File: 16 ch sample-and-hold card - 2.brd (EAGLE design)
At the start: 64 x 25.4 mm, 80 parts, among them IC1 TL074D, IC3 TL074D, IC4 TL074D, IC7 TL074D, IC9 MAX306CWI

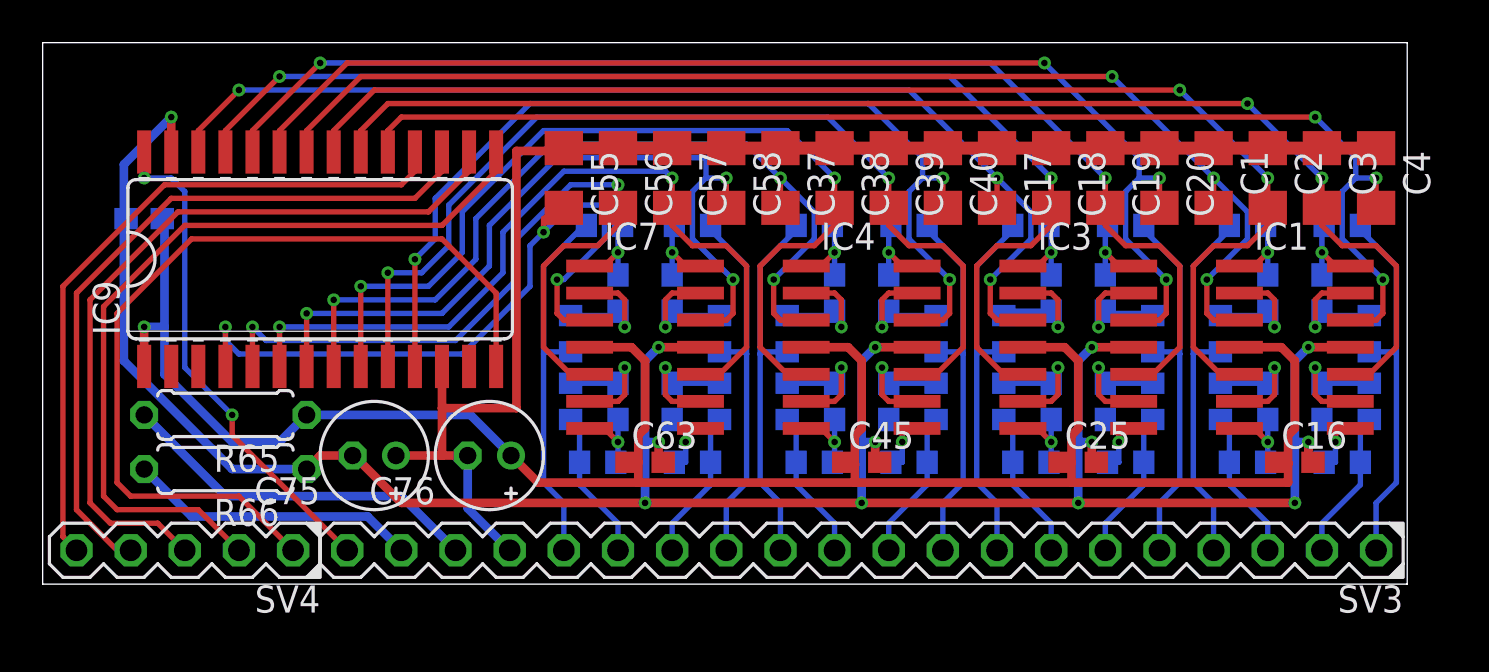
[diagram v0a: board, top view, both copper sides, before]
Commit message: Reworked resistor and electrolytic caps placement to tap power AFTER caps for better noise filtering
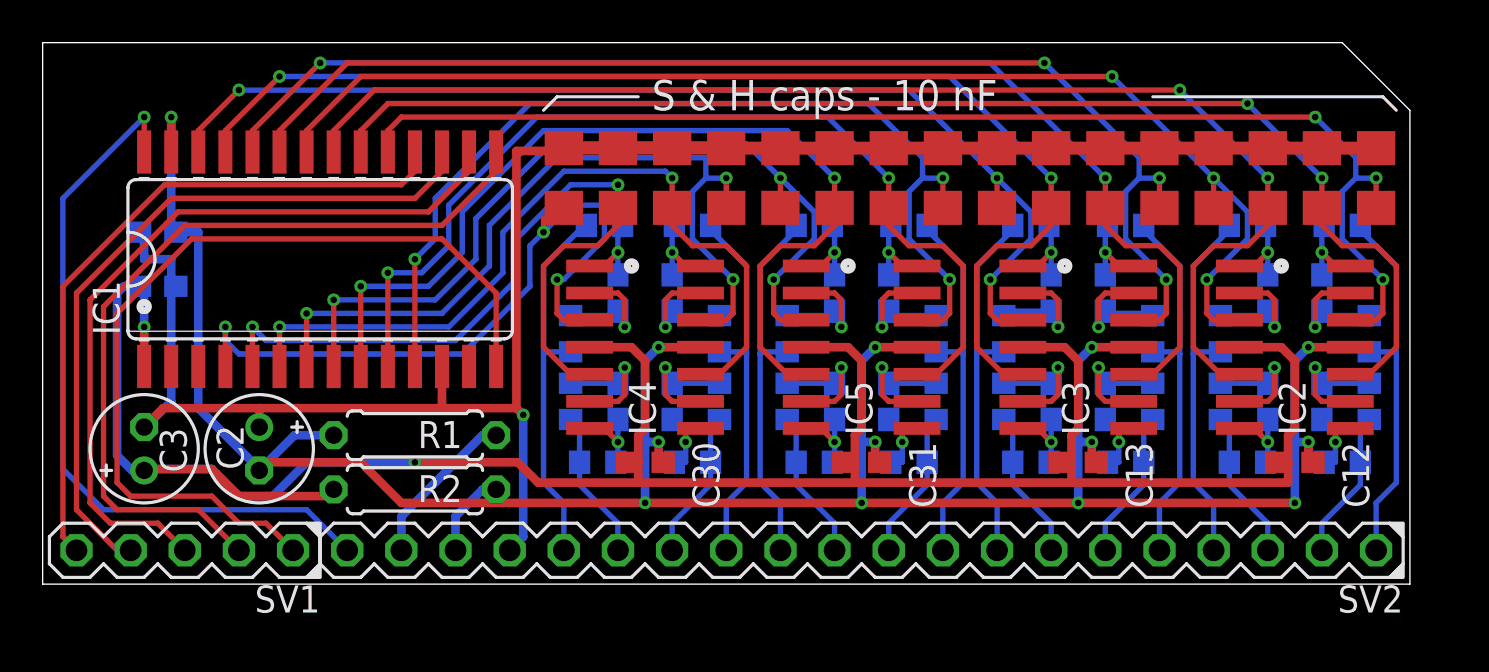
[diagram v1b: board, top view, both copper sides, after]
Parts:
- removed C41, C42, C43, C60, C61, C73: 0.1uF, resistor:C0603
- removed C55, C56, C57, C58: (no value), resistor:C1206
- removed C75, C76: 22uF 25V, resistor:E2-5
- removed IC7: TL074D, linear:SO14
- removed IC9: MAX306CWI, maxim:SO28L
- removed R51, R53, R56: 100R, resistor:R0603
- removed R52, R54, R55: 1k, resistor:R0603
- removed R65, R66: 100, resistor:0207/7
- added C10, C11, C26, C27, C28, C29, C7, C8, C9: 10nF, resistor:C1206
- added C12, C13, C14, C15: 0.1uF, resistor:C0603
- added IC2, IC5: TL074D, linear:SO14
- added R10, R12, R14, R16: 100R, resistor:R0603
- added R11, R13, R15, R9: 1k, resistor:R0603
- C1: value 10nF -> 0.1uF; device resistor:C1206 -> resistor:C0603
- C17, C18, C19, C20, C37, C38, C39, C40: value (none) -> 0.1uF; device resistor:C1206 -> resistor:C0603
- C2, C3: value (none) -> 22uF 25V; device resistor:C1206 -> resistor:E2-5
- C22, C23, C24, C25, C5, C6: value 0.1uF -> 10nF; device resistor:C0603 -> resistor:C1206
- C4: value (none) -> 10nF
- IC1: value TL074D -> MAX306CWI; device linear:SO14 -> maxim:SO28L
- R1: value 100R -> 100; device resistor:R0603 -> resistor:0207/7
- R17, R19, R21, R3, R33, R5: value 100R -> 1k
- R18, R20, R22, R34, R4, R6: value 1k -> 100R
- R2: value 1k -> 100; device resistor:R0603 -> resistor:0207/7
- moved C3 56.7 mm to (4.76, 6.35), turned to 90 degrees
- moved C1 49.6 mm to (5.40, 16.5), flipped to the bottom, turned to 0 degrees
- moved C2 49.0 mm to (10.2, 6.35)
- moved IC1 45.9 mm to (13.0, 15.2), turned to 0 degrees
- moved R1 40.3 mm to (17.5, 6.99), flipped to the top
- moved R2 38.5 mm to (17.5, 4.45), flipped to the top, turned to 0 degrees
- moved C40 37.2 mm to (5.40, 14.0), flipped to the bottom, turned to 0 degrees
- moved C34 30.5 mm to (27.0, 8.57)
- moved C33 28.4 mm to (29.5, 8.57), turned to 90 degrees
- moved C25 27.6 mm to (24.4, 19.1), turned to 270 degrees
- moved R23 27.5 mm to (24.8, 8.57)
- moved R24 27.1 mm to (26.0, 5.71), turned to 0 degrees
- moved C24 23.5 mm to (27.0, 19.1), flipped to the top
- moved C23 22.9 mm to (29.5, 19.1), flipped to the top, turned to 270 degrees
- moved R22 21.8 mm to (30.5, 5.71), turned to 180 degrees
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- renumbered C44 to C36, C45 to C31, C59 to C35, C62 to C32, C63 to C30, R35 to R32, R36 to R31, R37 to R30, R38 to R29, R39 to R27, R40 to R28, R49 to R26, R50 to R25, SV3 to SV2, SV4 to SV1
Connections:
- net +15V: now also C12.1, C13.1, C3.+, C40.2, IC1.1, IC2.4, IC5.4, R2.1; no longer C16.1, C25.1, C73.2, C76.+, IC1.4, IC7.4, IC9.1, R65.1
- net -15V: now also C1.1, C12.2, C13.2, C2.-, IC1.27, IC2.11, IC5.11, R1.1; no longer C16.2, C25.2, C73.1, C75.-, IC1.11, IC7.11, IC9.27, R66.1
- net A0: now also IC1.17; no longer IC9.17
- net A1: now also IC1.16; no longer IC9.16
- net A2: now also IC1.15; no longer IC9.15
- net A3: now also IC1.14; no longer IC9.14
- net AGND: now also C1.2, C10.1, C11.1, C2.+, C22.1, C23.1, C24.1, C25.1, C26.1, C27.1, C28.1, C29.1, C3.-, C5.1, C6.1, C7.1, C8.1, C9.1, IC1.12; no longer C1.1, C17.1, C18.1, C19.1, C2.1, C20.1, C3.1, C37.1, C38.1, C39.1, C55.1, C56.1, C57.1, C58.1, C75.+, C76.-, IC9.12
- net DAC: now also IC1.28; no longer IC9.28
- net EN: now also IC1.18; no longer IC9.18
- net IN1: now also IC1.19, IC2.12; no longer IC1.12, IC9.19
- net IN11: now also C9.2, IC1.24; no longer C19.2, IC9.24
- net IN12: now also C10.2, IC1.25; no longer C18.2, IC9.25
- net IN14: now also C11.2, IC1.26; no longer C17.2, IC9.26
- net IN17: now also C26.2, IC1.11, IC5.12; no longer C40.2, IC4.12, IC9.11
- net IN19: now also C27.2, IC1.10, IC5.10; no longer C39.2, IC4.10, IC9.10
- net IN20: now also C28.2, IC1.9, IC5.5; no longer C38.2, IC4.5, IC9.9
- net IN22: now also C29.2, IC1.8, IC5.3; no longer C37.2, IC4.3, IC9.8
- net IN25: now also C22.2, IC1.7, IC4.12; no longer C58.2, IC7.12, IC9.7
- net IN27: now also C23.2, IC1.6, IC4.10; no longer C57.2, IC7.10, IC9.6
- net IN28: now also C24.2, IC1.5, IC4.5; no longer C56.2, IC7.5, IC9.5
- net IN3: now also C5.2, IC1.20, IC2.10; no longer C3.2, IC1.10, IC9.20
- net IN30: now also C25.2, IC1.4, IC4.3; no longer C55.2, IC7.3, IC9.4
- net IN4: now also C6.2, IC1.21, IC2.5; no longer C2.2, IC1.5, IC9.21
- net IN6: now also C7.2, IC1.22, IC2.3; no longer C1.2, IC1.3, IC9.22
- net IN9: now also C8.2, IC1.23; no longer C20.2, IC9.23
- net N$1: now also C17.2, IC2.2, R9.1; no longer C33.2, IC1.2, R2.1
- net N$10: now also R17.1; no longer R18.1
- net N$19: now also C20.1, R16.1; no longer C22.1, R19.1
- net N$2: now also C17.1, IC2.1, R10.1; no longer C33.1, IC1.1, R1.1
- net N$20: now also C20.2, R15.1; no longer C22.2, R20.1
- net N$21: now also C19.1, R14.1; no longer C23.1, R21.1
- net N$22: now also C18.1, R12.1; no longer C24.1, R24.1
- net N$23: now also C19.2, R13.1; no longer C23.2, R22.1
- net N$24: now also C18.2, R11.1; no longer C24.2, R23.1
- net N$3: now also C16.1, IC2.7, R8.1; no longer C34.1, IC1.7, R3.1
- net N$33: now also C39.1, IC5.1, R34.1; no longer C41.1, IC4.1, R33.1
- net N$34: now also C39.2, IC5.2, R33.1; no longer C41.2, IC4.2, R34.1
- net N$35: now also C38.1, IC5.7; no longer C42.1, IC4.7
- net N$36: now also C38.2, IC5.6; no longer C42.2, IC4.6
- net N$37: now also C37.1, IC5.8; no longer C43.1, IC4.8
- net N$38: now also IC5.14; no longer IC4.14
- net N$39: now also C37.2, IC5.9; no longer C43.2, IC4.9
- net N$4: now also C15.1, IC2.8, R6.1; no longer C5.1, IC1.8, R5.1
- net N$40: now also IC5.13; no longer IC4.13
- net N$49: now also IC4.1; no longer IC7.1
- net N$5: now also C16.2, IC2.6, R7.1; no longer C34.2, IC1.6, R4.1
- net N$50: now also IC4.2; no longer IC7.2
- net N$51: now also C34.1, IC4.7, R24.1; no longer C60.1, IC7.7, R51.1
- net N$52: now also C34.2, IC4.6, R23.1; no longer C60.2, IC7.6, R52.1
- net N$53: now also C33.1, IC4.8, R22.1; no longer C61.1, IC7.8, R53.1
- net N$54: now also IC4.14, R20.1; no longer IC7.14, R56.1
- net N$55: now also C33.2, IC4.9, R21.1; no longer C61.2, IC7.9, R54.1
- net N$56: now also IC4.13, R19.1; no longer IC7.13, R55.1
- net N$6: now also C14.1, IC2.14, R4.1; no longer C6.1, IC1.14, R8.1
- net N$7: now also C15.2, IC2.9, R5.1; no longer C5.2, IC1.9, R6.1
- net N$8: now also C14.2, IC2.13, R3.1; no longer C6.2, IC1.13, R7.1
- net N$9: now also R18.1; no longer R17.1
- net OUT0: now also R3.2, R4.2; no longer R7.2, R8.2
- net OUT14: now also R15.2, R16.2; no longer R19.2, R20.2
- net OUT24: now also R19.2, R20.2; no longer R55.2, R56.2
- net OUT25: now also R21.2, R22.2; no longer R53.2, R54.2
- net OUT30: now also R23.2, R24.2; no longer R51.2, R52.2
- net OUT6: now also R7.2, R8.2; no longer R3.2, R4.2
- net OUT7: now also R10.2, R9.2; no longer R1.2, R2.2
- net OUT8: now also R11.2, R12.2; no longer R23.2, R24.2
- net OUT9: now also R13.2, R14.2; no longer R21.2, R22.2
- net V+: now also R2.2; no longer R65.2
- net V-: now also R1.2; no longer R66.2
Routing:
- net AGND: track 69.9 -> 92.0 mm, vias 0 -> 1
- net V+: track 17.2 -> 4.02 mm
- net +15V: track 104.3 -> 117.3 mm, vias 1 -> 2
- net DAC: track 23.4 -> 34.6 mm, vias 2 -> 1
- net V-: track 13.6 -> 7.61 mm
- net -15V: track 118.3 -> 120.0 mm
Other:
- board size 64 x 25.4 mm -> 64.1 x 25.4 mm
- board text added: "S & H caps - 10 nF"

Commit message: Last commit before moving multiplexer to separate repo
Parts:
- added C41, C42, C43, C44: 0.1uF, resistor:C0603
- R1, R2: value 100 -> 100R
- moved C12 3.62 mm to (55.2, 4.76), turned to 270 degrees
- moved C13 3.62 mm to (45.1, 4.76), turned to 270 degrees
- moved C30 3.62 mm to (24.8, 4.76), turned to 270 degrees
- moved C31 3.62 mm to (34.9, 4.76), turned to 270 degrees
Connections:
- net -15V: now also C41.2, C42.2, C43.2, C44.2; no longer C12.2, C13.2, C30.2, C31.2
- net AGND: now also C12.2, C13.2, C30.2, C31.2, C41.1, C42.1, C43.1, C44.1
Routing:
- net AGND: track 92.0 -> 130.0 mm, vias 1 -> 2
- net +15V: track 117.3 -> 107.9 mm
- net -15V: track 120.0 -> 121.2 mm
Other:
- board text added: "0.1u"
- board text added: "100R"
- board text added: "1k"
- board text added: "22u 25v"
- board text added: "S & H caps - 10n"
- board text removed: "S & H caps - 10 nF"
